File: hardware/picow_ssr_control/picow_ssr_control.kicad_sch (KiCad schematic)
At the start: 39 parts, among them Q1 IRF4905PBF, Q2 DMG2301L, U1 RaspberryPi-PicoW

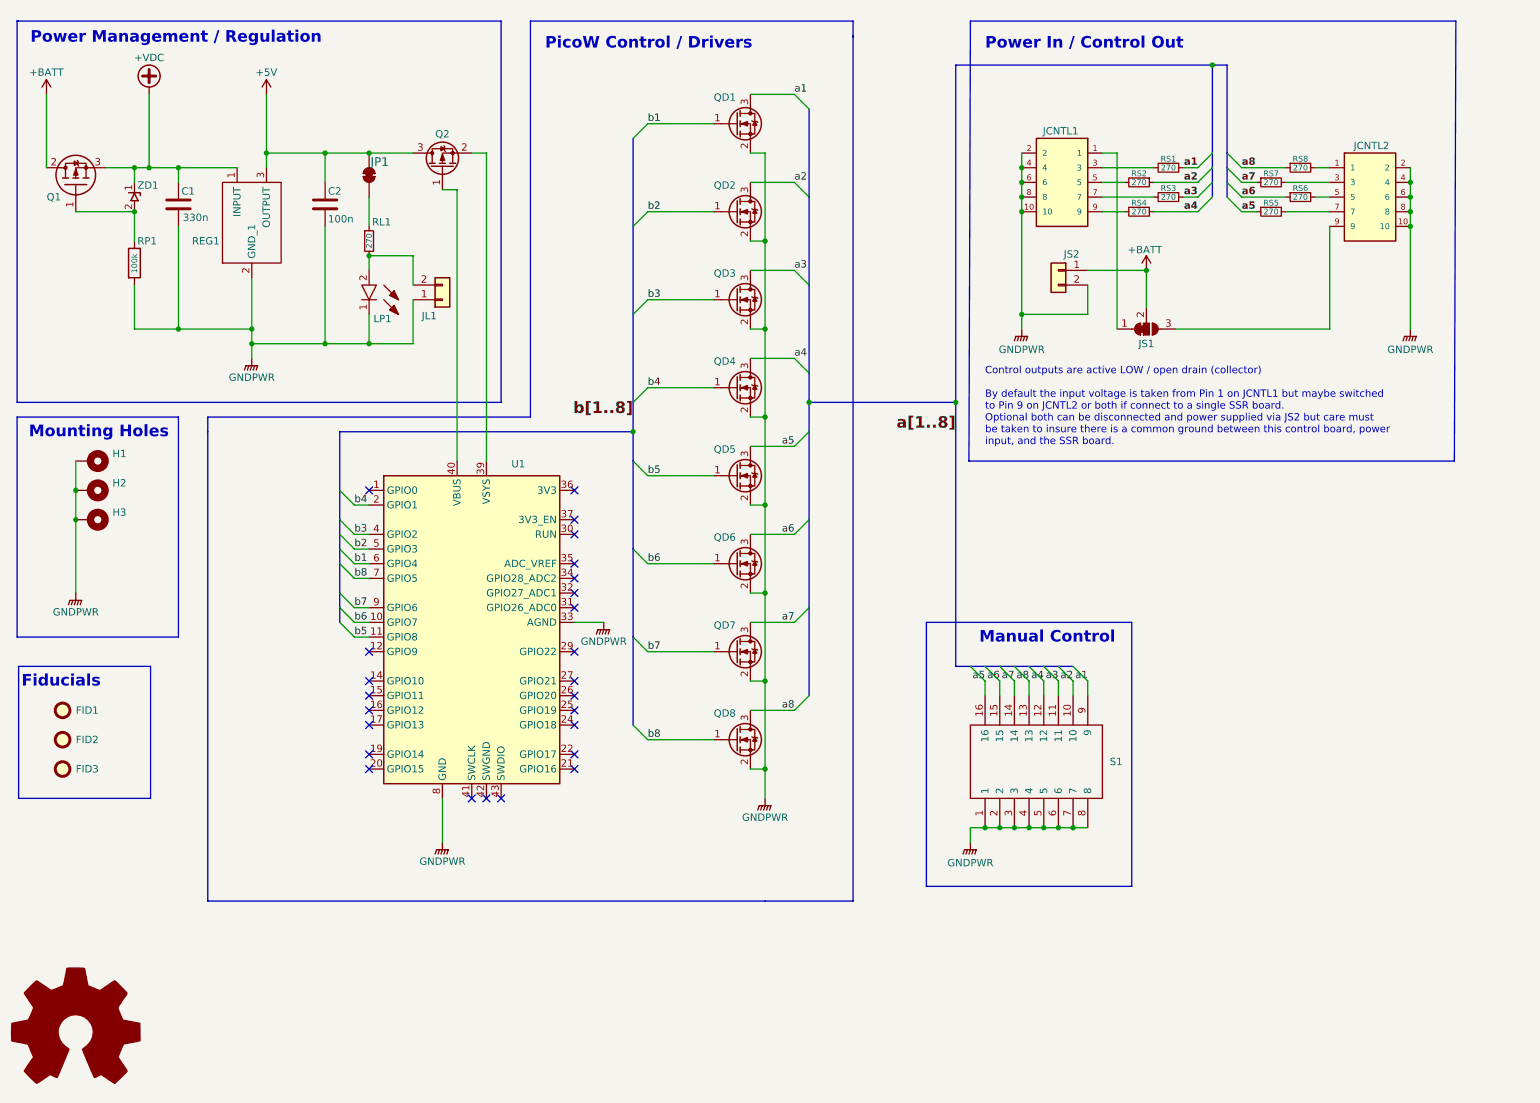
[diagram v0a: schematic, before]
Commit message: Added pulldowns to driver FETs and realigned control connectors and other components
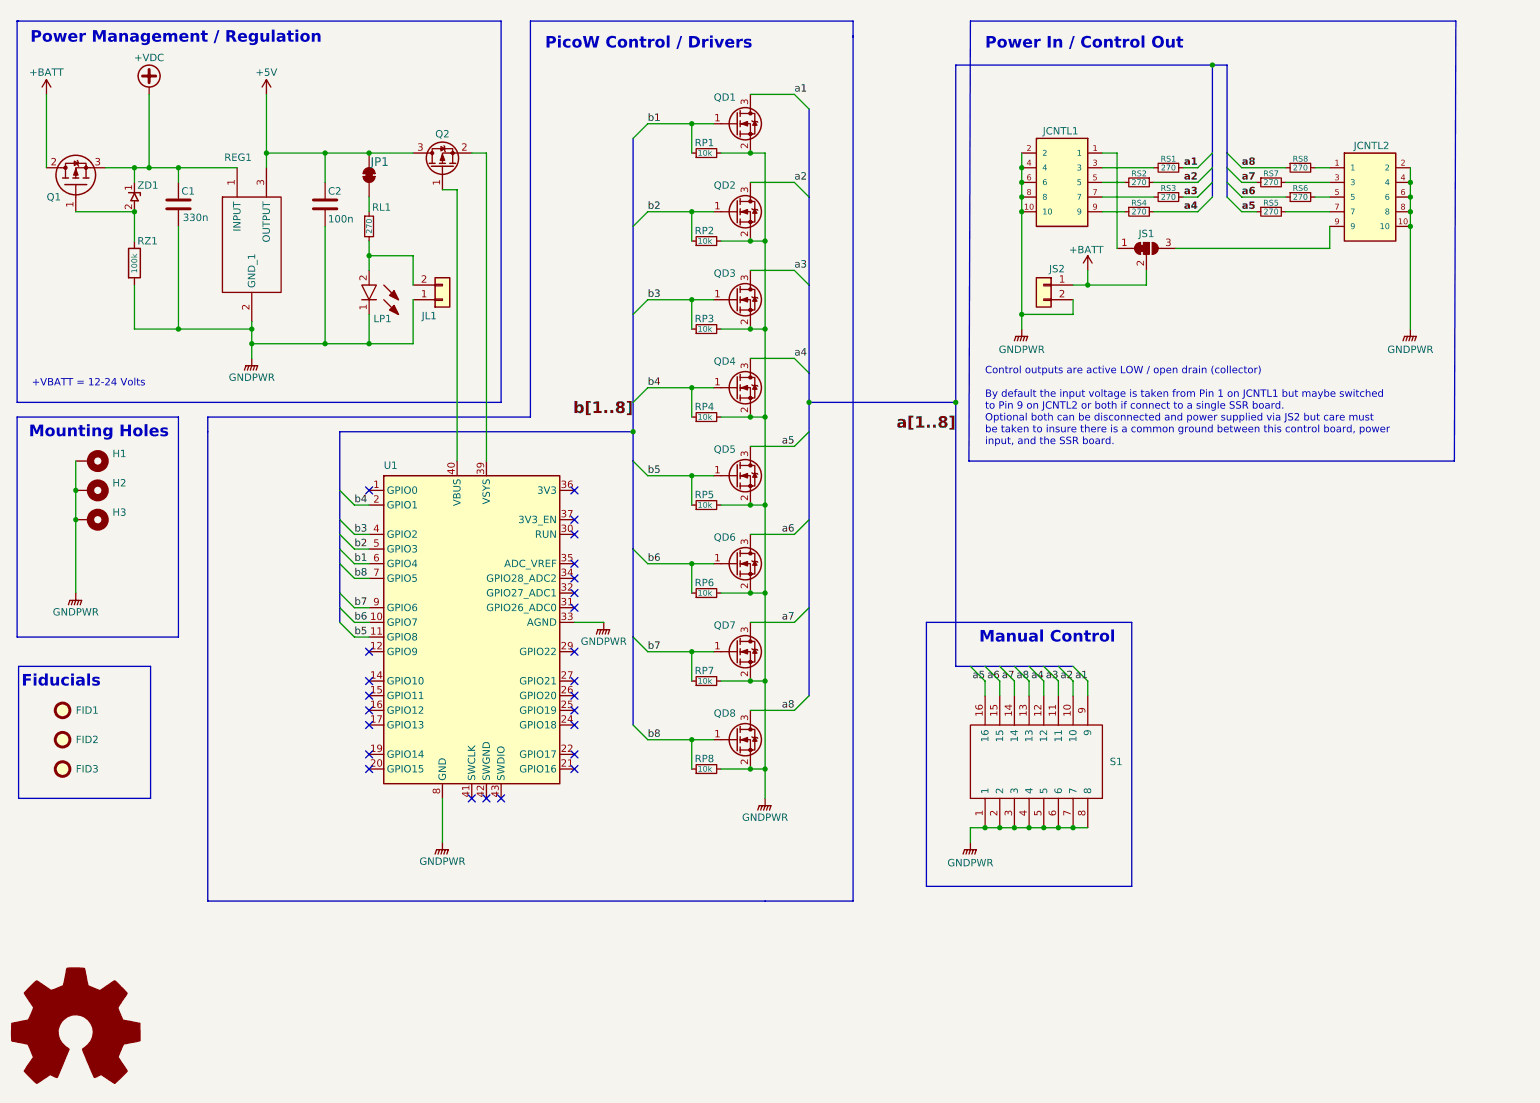
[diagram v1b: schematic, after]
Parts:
- removed REG1: LM7805, SOT230P700X180-4N, symbol SamacSys_Parts:LM7805MPX_NOPB
- added REG1: LM7805, Package_TO_SOT_SMD:SOT-223, symbol We_control:LM7805MPX_NOPB
- added RP1, RP2, RP3, RP4, RP5, RP6, RP7, RP8: 10k, Resistor_SMD:R_0603_1608Metric, symbol Device:R_Small
- JCNTL1, JCNTL2: symbol Connector_Samtec:SHF-105-01-L-D-RA -> dragon_mobile:SHF-105-01-L-D-RA; Height (mm) (none) -> 5.33; MANUFACTURER Samtec -> (none); MFN (none) -> Samtec; MFP (none) -> SHF-105-01-L-D-RA-TR; Mouser Part Number (none) -> 200-SHF10501LDRATR; Mouser Price/Stock (none) -> https://www.mouser.com/ProductDetail/Samtec/SHF-105-01-L-D-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; PARTREV R -> (none); STANDARD Manufacturer Recommendations -> (none); Type (none) -> THT
- Q2: footprint Picow_control:DMG2301L -> Package_TO_SOT_SMD:SOT-23; symbol Picow_control:DMG2301L -> dragon_mobile:DMG2301L
- S1: footprint Picow_control:1938MS -> dragon_mobile:1938MS; symbol Picow_control:193-8MS -> dragon_mobile:193-8MS; Height (none) -> 9.37; Manufacturer_Name (none) -> CTS; Manufacturer_Part_Number (none) -> 193-8MS; Mouser Part Number (none) -> 774-1938MS
- U1: footprint Pico:Raspberry_Pi_Pico_THT -> dragon_mobile:Raspberry_Pi_Pico_THT; symbol Pico:RaspberryPi-PicoW -> dragon_mobile:RaspberryPi-PicoW
- ZD1: footprint Picow_control:BZD27C10P-M3-08 -> dragon_mobile:BZD27C10P-M3-08; symbol Picow_control:BZD27C10P-M3-08 -> dragon_mobile:BZD27C10P-M3-08
- renumbered RP1 to RZ1
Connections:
- net +5V: now also REG1.3 (OUTPUT)
- net +VDC: now also REG1.1 (INPUT)
- net GNDPWR: now also REG1.2 (GND_1), REG1.4 (GND_2), RP1.2, RP2.2, RP3.2, RP4.2, RP5.2, RP6.2, RP7.2, RP8.2
- net b1: now also RP1.1
- net b2: now also RP2.1
- net b3: now also RP3.1
- net b4: now also RP4.1
- net b5: now also RP5.1
- net b6: now also RP6.1
- net b7: now also RP7.1
- net b8: now also RP8.1
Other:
- note added: "+VBATT = 12-24 Volts"
- moved on the sheet: JS1, JS2, RL1
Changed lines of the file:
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@@
   (title_block
     (title "Picow SSR Control")
-    (date "2023-01-02")
-    (rev "0.0.8")
+    (date "2023-01-23")
+    (rev "0.0.9")
     (comment 2 "http://creativecommons.org/licenses/by-sa/4.0/")
     (comment 3 "License: CC By SA 4.0")

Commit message: Changed schematic to hierarchical style with mutliple sheets
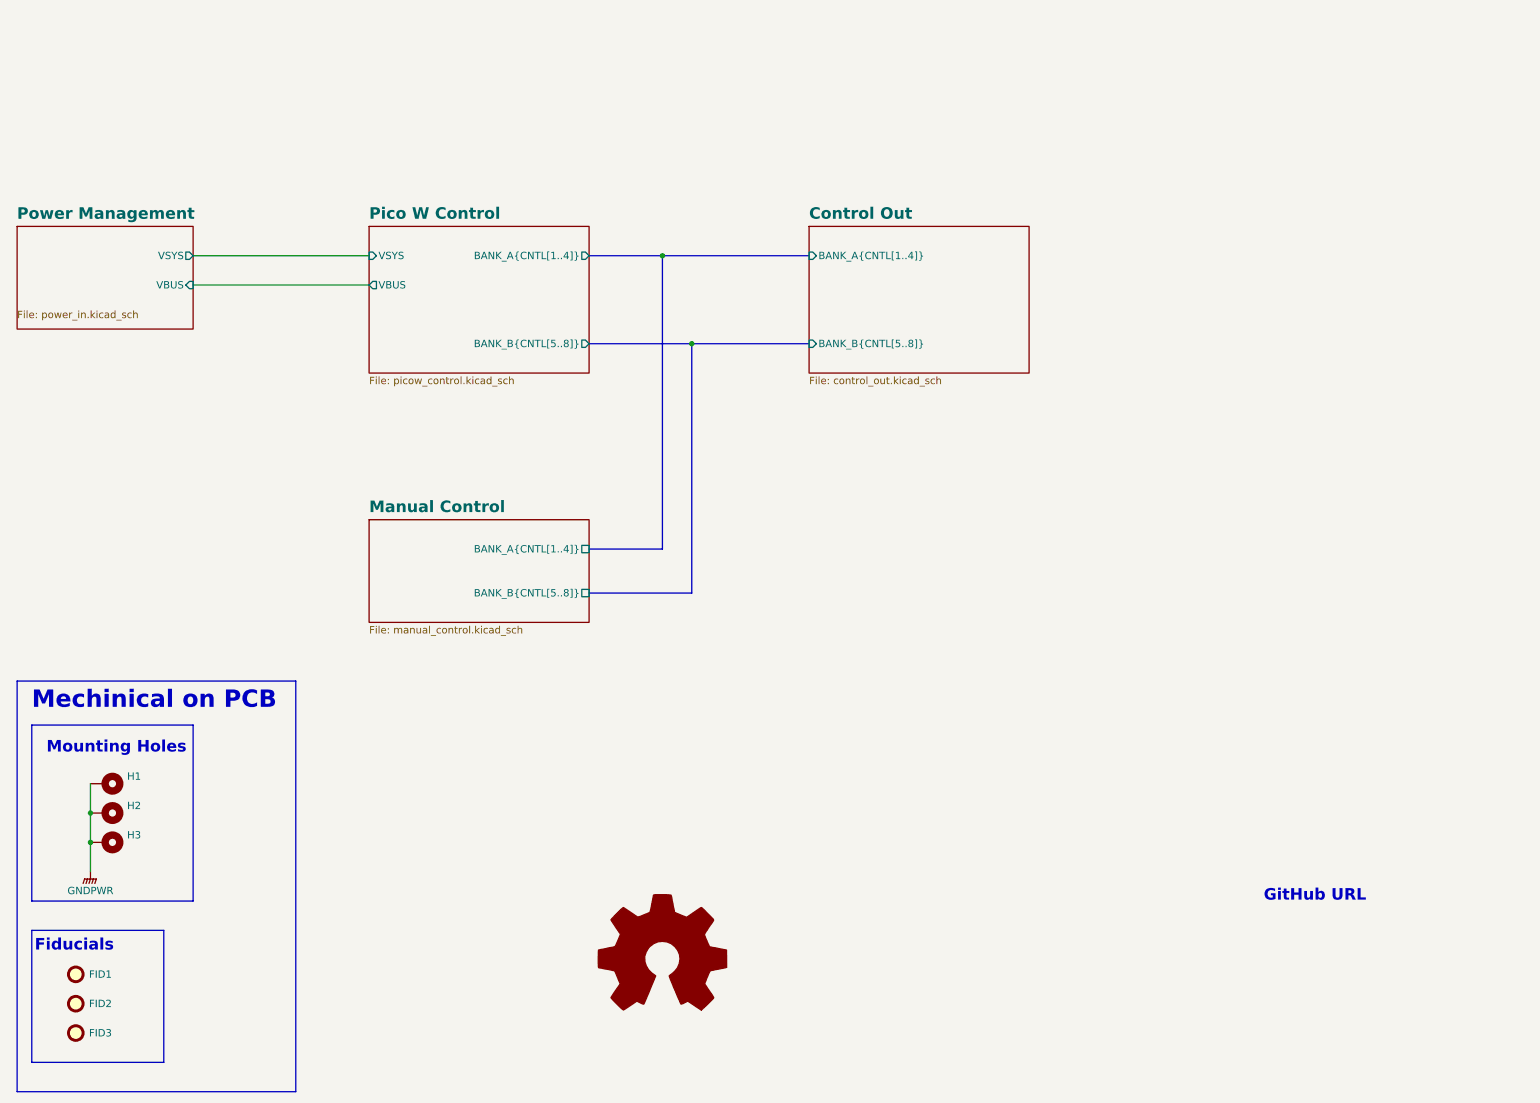
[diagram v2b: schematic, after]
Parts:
- removed C1: 330n, Capacitor_SMD:C_0805_2012Metric, symbol Device:C
- removed C2: 100n, Capacitor_SMD:C_0805_2012Metric, symbol Device:C
- removed JCNTL1, JCNTL2: SHF-105-01-L-D-RA, dragon_mobile:SAMTEC_SHF-105-01-L-D-RA, symbol dragon_mobile:SHF-105-01-L-D-RA
- removed JL1, JS2: Conn_01x02, Connector_PinHeader_1.00mm:PinHeader_1x02_P1.00mm_Vertical, symbol Connector_Generic:Conn_01x02
- removed JP1: SolderJumper_2_Bridged, Jumper:SolderJumper-2_P1.3mm_Bridged_RoundedPad1.0x1.5mm, symbol Jumper:SolderJumper_2_Bridged
- removed JS1: SolderJumper_3_Bridged12, Jumper:SolderJumper-3_P1.3mm_Bridged12_RoundedPad1.0x1.5mm_NumberLabels, symbol Jumper:SolderJumper_3_Bridged12
- removed LP1: LTST-C190KGKT, dragon_mobile:LEDC1608X80N, symbol dragon_mobile:LTST-C190KGKT
- removed Q1: IRF4905PBF, dragon_mobile:TO254P469X1042X1967-3P, symbol dragon_mobile:IRF4905PBF
- removed Q2: DMG2301L, Package_TO_SOT_SMD:SOT-23, symbol dragon_mobile:DMG2301L
- removed QD1, QD2, QD3, QD4, QD5, QD6, QD7, QD8: 2N7002K, Package_TO_SOT_SMD:SOT-23, symbol Transistor_FET:2N7002K
- removed REG1: LM7805, Package_TO_SOT_SMD:SOT-223, symbol We_control:LM7805MPX_NOPB
- removed RL1, RS1, RS2, RS3, RS4, RS5, RS6, RS7, RS8: 270, Resistor_SMD:R_0603_1608Metric, symbol Device:R_Small
- removed RP1, RP2, RP3, RP4, RP5, RP6, RP7, RP8: 10k, Resistor_SMD:R_0603_1608Metric, symbol Device:R_Small
- removed RZ1: 100k, Resistor_SMD:R_0805_2012Metric, symbol Device:R
- removed S1: 193-8MS, dragon_mobile:1938MS, symbol dragon_mobile:193-8MS
- removed U1: RaspberryPi-PicoW, dragon_mobile:Raspberry_Pi_Pico_THT, symbol dragon_mobile:RaspberryPi-PicoW
- removed ZD1: +10v Zener Diode, dragon_mobile:BZD27C10P-M3-08, symbol dragon_mobile:BZD27C10P-M3-08
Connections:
- no-connect marks 25 -> 0
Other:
- added sheet Control Out (control_out.kicad_sch)
- added sheet Manual Control (manual_control.kicad_sch)
- added sheet Pico W Control (picow_control.kicad_sch)
- added sheet Power Management (power_in.kicad_sch)
- note added: "GitHub URL"
- note added: "Mechinical on PCB"
- note removed: "+VBATT = 12-24 Volts"
- note removed: "Control outputs are active LOW / open drain (collector) By default the input voltage is taken from Pin 1 on JCNTL1 but maybe switched to Pin 9 on JCNTL2 or both if connect to a single SSR board. Optional both can be disconnected and power supplied via JS2 but care must be taken to insure there is a common ground between this control board, power input, and the SSR board."
- note removed: "Manual Control"
- note removed: "PicoW Control / Drivers"
- note removed: "Power In / Control Out"
- note removed: "Power Management / Regulation"
- moved on the sheet: FID1, FID2, FID3, H1, H2, H3
